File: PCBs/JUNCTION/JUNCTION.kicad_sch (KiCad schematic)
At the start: 10 parts, among them J1 JUNC, J2 TSMP, J3 HV, J4 HVD_IN, J5 HALL, U1 AMS1117-5.0

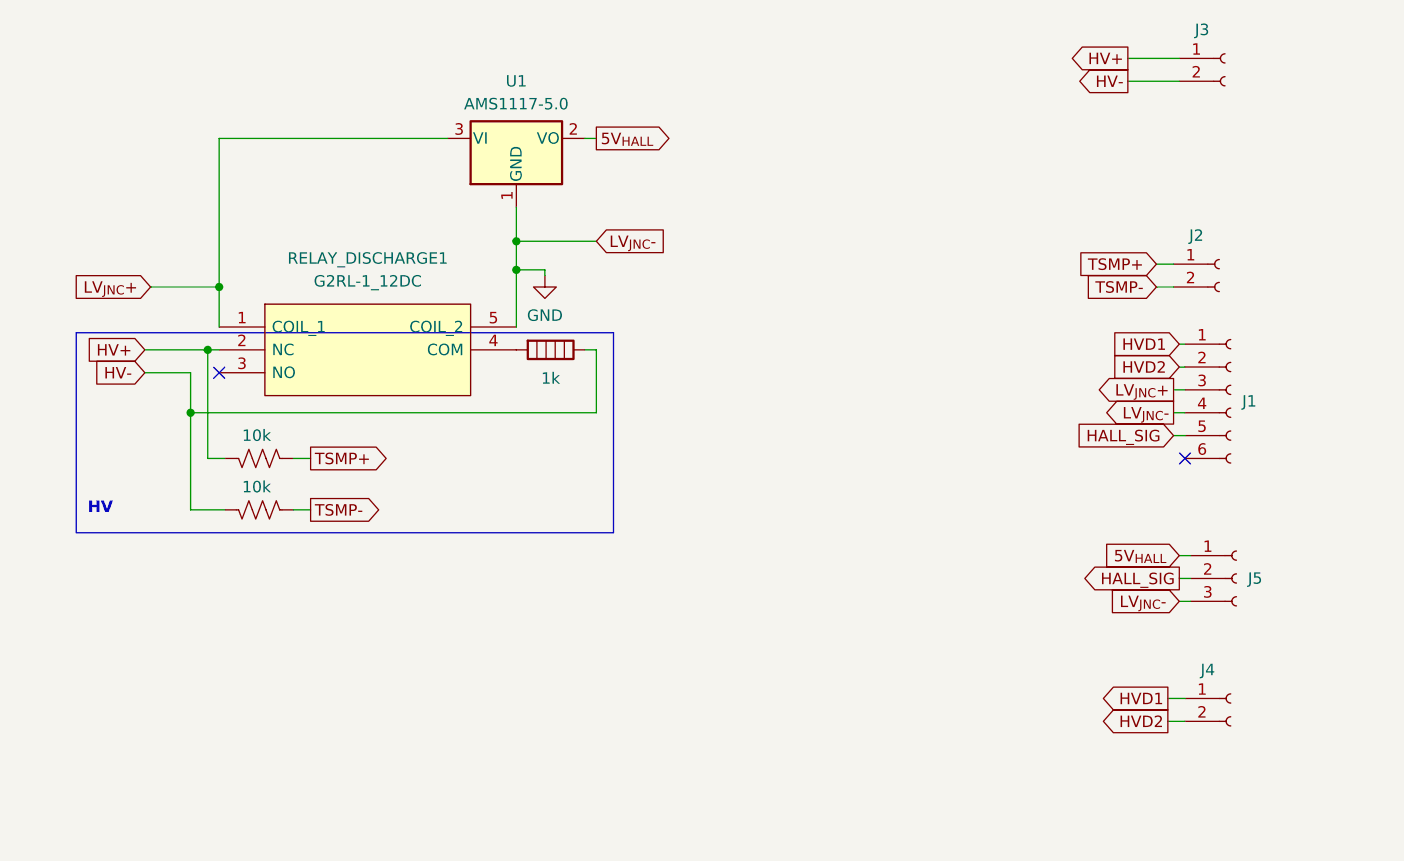
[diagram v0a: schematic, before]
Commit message: update: schematics and wirings to current state
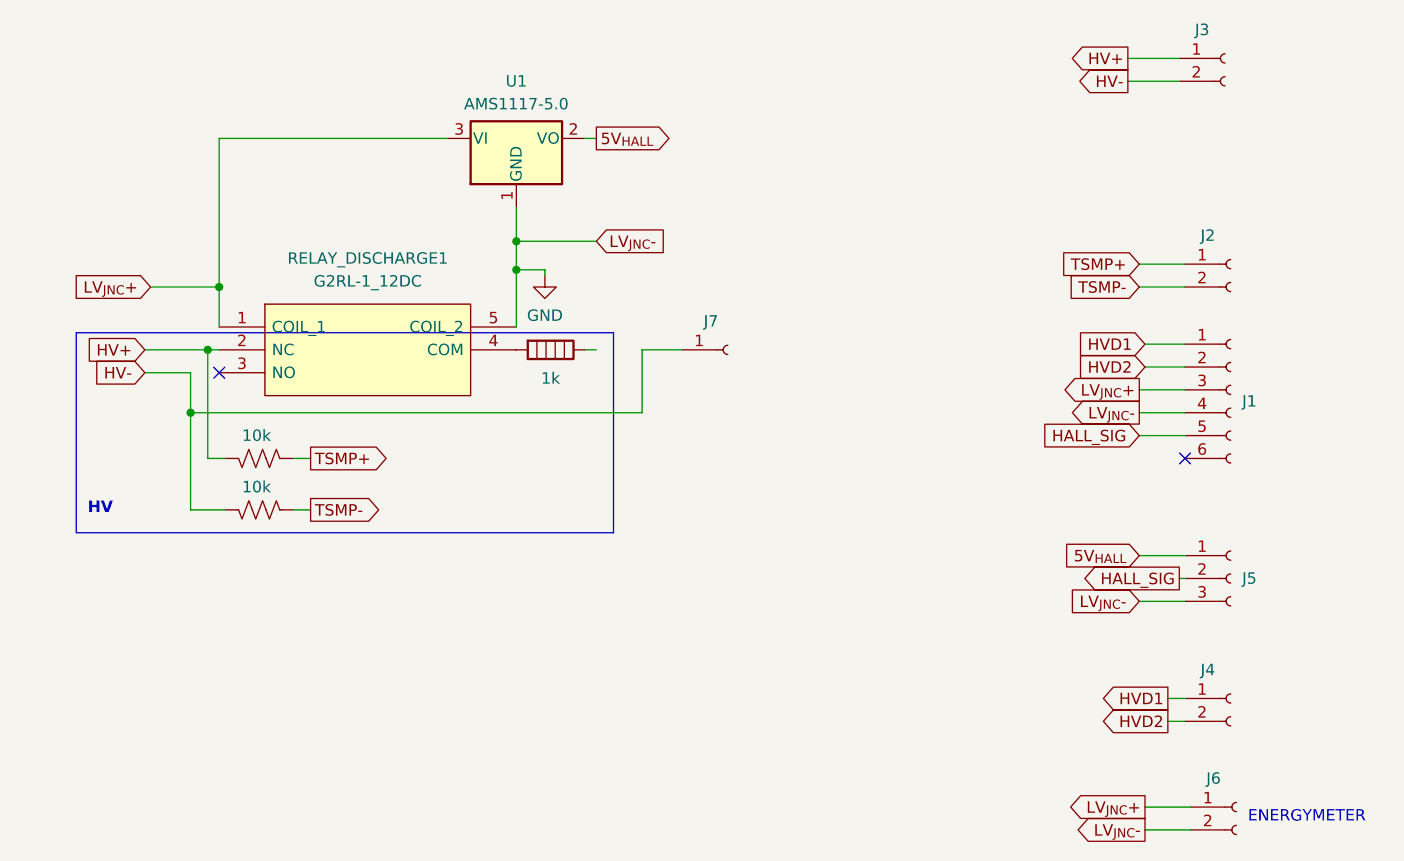
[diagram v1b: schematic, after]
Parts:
- added J6: ENERGYMETER, Connector_PinHeader_2.54mm:PinHeader_1x02_P2.54mm_Vertical, symbol A-FA_PARTS:Conn_01x02_Female
- added J7: R_DISCHARGE, Connector_PinHeader_2.54mm:PinHeader_1x01_P2.54mm_Vertical, symbol 11:Conn_01x01_Female
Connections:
- net GND: now also J6.2 (Pin_2)
- net HV-: now also J7.1 (Pin_1); no longer R_DIS_place_in_pcb1.1
- net LV_{JNC}+: now also J6.1 (Pin_1)
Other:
- note added: "ENERGYMETER"
- moved on the sheet: J2, J5
